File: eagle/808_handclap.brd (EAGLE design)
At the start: 100 x 80 mm, 82 parts, among them IC1 LM339N, IC2 TL071P, IC3 TL071P, Q1 2N3906, Q2 2N3904, Q3 2N3906, Q4 2N3906, Q5 2N3904, Q6 2N3904, Q7 2N3904, U1 POWER, U22 BA6110SIL

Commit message: 88pct autorouted
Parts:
- R350, R356, R364, R367, R371: device TR808clone:0207/5V -> TR808clone:0207/7
- moved C138 5.24 mm to (26.7, 69.8), turned to 270 degrees
- moved C140 4.02 mm to (48.3, 17.8)
- moved R363 2.84 mm to (7.62, 53.3)
- moved C139 2.54 mm to (33.0, 67.3), turned to 270 degrees
- moved Q7 2.54 mm to (49.5, 25.4)
- moved C144 2.54 mm to (50.8, 12.7)
- moved R367 2.54 mm to (43.2, 17.8)
- moved R368 2.54 mm to (39.4, 22.9)
- moved R348 1.80 mm to (29.2, 69.8), turned to 270 degrees
- moved C143 1.80 mm to (31.8, 54.6)
- moved D71 1.80 mm to (58.4, 8.89)
- moved R373 1.80 mm to (30.5, 15.2)
- moved C142 1.80 mm to (68.6, 27.9), turned to 0 degrees
- moved TM3 1.27 mm to (19.1, 73.7), turned to 90 degrees
- moved R358 1.27 mm to (58.4, 25.4)
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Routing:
- net GND: track 391.3 -> 0.00 mm
- net +12V: track 315.0 -> 0.00 mm
- net -12V: track 262.2 -> 0.00 mm
- net N$92: track 211.9 -> 0.00 mm
- net N$75: track 52.3 -> 0.00 mm
- net N$78: track 39.0 -> 0.00 mm
- net N$42: track 33.5 -> 0.00 mm
- net N$68: track 29.5 -> 0.00 mm
- net N$73: track 29.2 -> 0.00 mm
- net N$72: track 28.1 -> 0.00 mm
- net N$49: track 27.4 -> 0.00 mm
- net N$74: track 25.4 -> 0.00 mm
- net N$40: track 24.3 -> 0.00 mm
- net N$10: track 20.9 -> 0.00 mm
- net N$97: track 19.8 -> 0.00 mm
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
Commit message: 88pct autorouted
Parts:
- R105: device TR808clone:0207/5V -> TR808clone:0207/2V
- R334: device TR808clone:0207/7 -> TR808clone:0309/10
- moved R357 20.9 mm to (86.4, 11.4), turned to 180 degrees
- moved R359 3.59 mm to (39.4, 8.89)
- moved C144 2.84 mm to (49.5, 10.2)
- moved Q1 1.80 mm to (45.7, 25.4)
- moved D68 1.27 mm to (41.9, 55.9)
- moved R346 1.27 mm to (34.3, 59.7)
- moved R367 1.27 mm to (43.2, 16.5)
- moved C136 1.27 mm to (44.5, 47.0)
- moved Q7 1.27 mm to (50.8, 25.4)
- turned Q4 to 90 degrees
- turned TM3 to 0 degrees

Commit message: manual mode
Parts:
- C142: device TR808clone:C025-025X050 -> TR808clone:C050-025X075
- D69, D70, D71: value 1N4148DO35-7 -> 1N4148DO35-10; device TR808clone:DO35-7 -> TR808clone:DO35-10
- R104, R200', R332, R348, R357, R366, R372, R378, R382: device TR808clone:0207/5V -> TR808clone:0207/7
- R352, R370: device TR808clone:0207/5V -> TR808clone:0309/10
- R356: device TR808clone:0207/7 -> TR808clone:0207/5V
- R359, R360, R373: device TR808clone:0309/10 -> TR808clone:0207/7
- R361, R369, R383: device TR808clone:0207/5V -> TR808clone:0207/2V
- R364: device TR808clone:0207/7 -> TR808clone:0309/10
- moved R357 27.4 mm to (59.7, 17.8), turned to 270 degrees
- moved R359 26.8 mm to (60.6, 25.3)
- moved R374 10.7 mm to (53.1, 32.6), turned to 270 degrees
- moved R373 4.49 mm to (31.1, 19.7), turned to 180 degrees
- moved R356 4.07 mm to (54.6, 14.6)
- moved R383 4.02 mm to (57.1, 35.6), turned to 90 degrees
- moved Q6 3.81 mm to (14.0, 61.0), turned to 180 degrees
- moved R358 3.59 mm to (61.0, 27.9)
- moved R363 3.59 mm to (10.2, 55.9)
- moved R368 3.59 mm to (41.9, 25.4)
- moved C141 2.84 mm to (86.4, 16.5), turned to 0 degrees
- moved R355 2.84 mm to (86.4, 21.6)
- moved WHITE_NORM 2.84 mm to (19.1, 38.1)
- moved R370 2.84 mm to (17.8, 61.0)
- moved C136 2.84 mm to (45.7, 49.5), turned to 90 degrees
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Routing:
- net GND: track 0.00 -> 537.8 mm, vias 0 -> 2
- net -12V: track 0.00 -> 224.4 mm
- net N$92: track 0.00 -> 215.8 mm
- net +12V: track 0.00 -> 140.6 mm
- net N$74: track 0.00 -> 60.3 mm
- net N$42: track 0.00 -> 51.2 mm
- net N$73: track 0.00 -> 40.2 mm
- net N$10: track 0.00 -> 38.5 mm
- net N$68: track 0.00 -> 29.1 mm
- net N$52: track 0.00 -> 26.4 mm
- net N$72: track 0.00 -> 25.6 mm
- net N$65: track 0.00 -> 25.3 mm
- net N$97: track 0.00 -> 21.2 mm
- net N$77: track 0.00 -> 18.6 mm
- net N$46: track 0.00 -> 18.1 mm
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
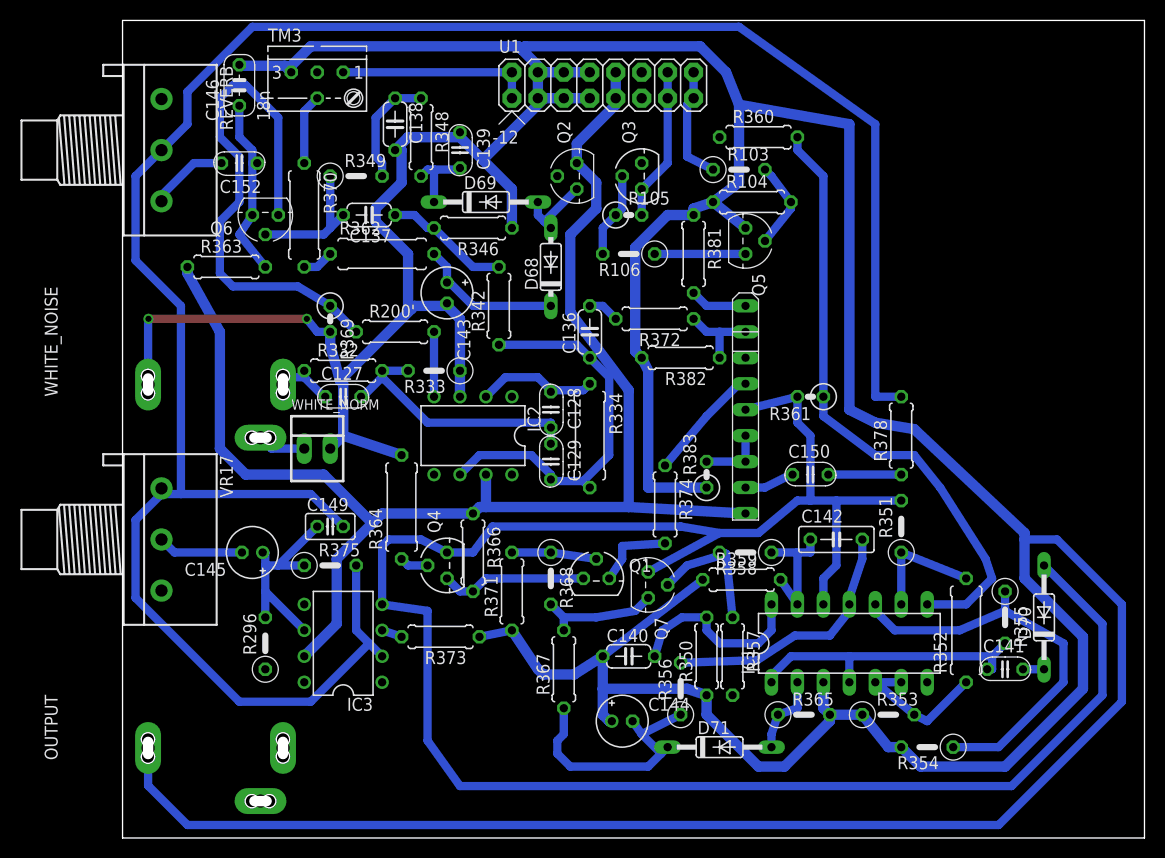
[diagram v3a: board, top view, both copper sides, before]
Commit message: more hand routes
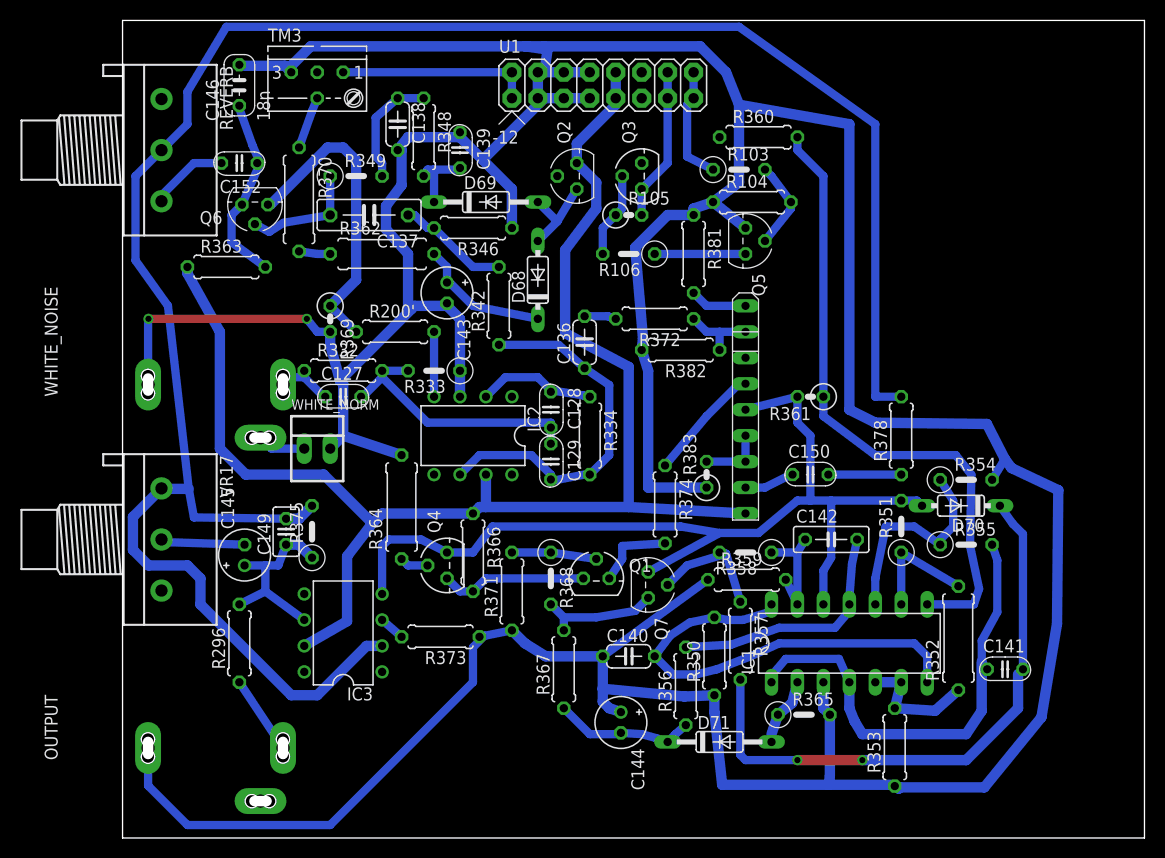
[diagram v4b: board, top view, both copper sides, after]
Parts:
- C137: device TR808clone:C050-024X044 -> TR808clone:C075-032X103
- D70: value 1N4148DO35-10 -> 1N4148DO35-7; device TR808clone:DO35-10 -> TR808clone:DO35-7
- R296, R353, R356: device TR808clone:0207/5V -> TR808clone:0207/7
- R334: device TR808clone:0309/10 -> TR808clone:0207/7
- moved R354 26.4 mm to (82.5, 35.1), turned to 0 degrees
- moved D70 13.6 mm to (82.0, 32.5), turned to 180 degrees
- moved R355 8.07 mm to (82.5, 28.7), turned to 0 degrees
- moved C149 4.35 mm to (16.0, 30.0), turned to 90 degrees
- moved R375 3.75 mm to (18.5, 30.0), turned to 90 degrees
- moved R353 3.24 mm to (75.6, 8.89), turned to 90 degrees
- moved R296 2.54 mm to (11.4, 19.1)
- moved D68 1.80 mm to (40.6, 54.6)
- moved R357 1.70 mm to (60.5, 19.3)
- moved R370 1.61 mm to (17.3, 62.5)
- moved Q6 1.44 mm to (13.0, 62.0)
- moved C136 1.14 mm to (45.2, 48.5)
- moved R352 1.08 mm to (81.8, 19.6)
- moved IC3 1.02 mm to (21.6, 20.1)
- moved C145 0.80 mm to (11.9, 27.7), turned to 90 degrees
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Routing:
- net -12V: track 224.4 -> 121.1 mm
- net GND: track 537.8 -> 468.1 mm
- net N$76: track 2.06 -> 57.7 mm, vias 0 -> 2
- net N$77: track 18.6 -> 44.6 mm
- net N$42: track 51.2 -> 30.3 mm
- net N$73: track 40.2 -> 20.9 mm
- net N$68: track 29.1 -> 46.5 mm
- net N$92: track 215.8 -> 203.8 mm
- net N$65: track 25.3 -> 13.8 mm
- net N$1: track 0.00 -> 7.72 mm
- net N$97: track 21.2 -> 18.6 mm
- net N$74: track 60.3 -> 62.5 mm
- net N$64: track 14.3 -> 12.2 mm
- net N$40: track 13.5 -> 11.7 mm
- net N$49: track 6.88 -> 5.14 mm
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
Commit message: routed
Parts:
- C127: device TR808clone:C035-025X75 -> TR808clone:C075-032X103
- C145: device TR808clone:E2-5 -> TR808clone:E3,5-8
- C149: device TR808clone:C025-025X050 -> TR808clone:C050-024X044
- R103, R368: device TR808clone:0207/5V -> TR808clone:0207/7
- R105: device TR808clone:0207/2V -> TR808clone:0207/5V
- R369: device TR808clone:0207/2V -> TR808clone:0207/7
- R381, R382: device TR808clone:0207/7 -> TR808clone:0207/5V
- moved R360 5.00 mm to (57.7, 66.5)
- moved R369 3.66 mm to (18.3, 53.8), turned to 180 degrees
- moved Q2 3.30 mm to (41.1, 64.8), turned to 0 degrees
- moved R349 3.10 mm to (20.3, 66.5), turned to 90 degrees
- moved R103 3.07 mm to (59.1, 62.6)
- moved Q5 2.75 mm to (59.4, 56.1)
- moved R378 2.54 mm to (73.7, 39.4)
- moved R334 2.17 mm to (43.7, 38.6)
- moved R106 2.09 mm to (50.0, 55.1)
- moved R375 2.05 mm to (20.6, 29.7)
- moved R104 2.05 mm to (61.3, 60.2)
- moved R363 1.83 mm to (11.7, 54.9), turned to 90 degrees
- moved R381 1.78 mm to (55.9, 55.4)
- moved C149 1.48 mm to (17.3, 29.2)
- moved R368 1.48 mm to (41.1, 24.1)
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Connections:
- net N$52: now also C127.2; no longer C127.P$2
- net WN: now also C127.1; no longer C127.P$1
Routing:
- net N$48: track 5.87 -> 100.6 mm, vias 0 -> 2
- net -12V: track 121.1 -> 189.9 mm, vias 0 -> 2
- net N$43: track 0.00 -> 14.0 mm
- net GND: track 468.1 -> 461.9 mm, vias 2 -> 4
- net N$42: track 30.3 -> 24.2 mm
- net N$46: track 18.9 -> 14.1 mm
- net TRIG: track 15.0 -> 18.9 mm
- net CP: track 11.4 -> 14.6 mm
- net N$78: track 11.8 -> 8.98 mm
- net N$44: track 9.09 -> 6.47 mm
- net N$62: track 7.14 -> 4.60 mm
- net N$52: track 26.4 -> 24.0 mm
- net N$60: track 11.4 -> 13.8 mm
- net N$37: track 8.41 -> 10.6 mm
- net N$3: track 8.89 -> 6.86 mm
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
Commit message: tweaks
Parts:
- R383: device TR808clone:0207/2V -> TR808clone:0207/7
- moved R383 6.14 mm to (56.4, 41.9), turned to 270 degrees
- moved R382 1.80 mm to (52.6, 48.3)
- moved R372 1.63 mm to (50.8, 51.1)
- moved R374 1.27 mm to (51.8, 32.9)
- moved R103 1.02 mm to (60.1, 62.6)
- moved R366 0.92 mm to (35.1, 28.4)
- moved Q1 0.80 mm to (46.1, 25.7)
- moved R334 0.51 mm to (43.7, 39.1)
- moved R359 0.51 mm to (61.6, 25.3)
- moved C128 0.25 mm to (41.1, 41.1)
- moved R369 0.25 mm to (18.5, 53.8)
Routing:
- net GND: track 461.9 -> 450.3 mm
- net N$60: track 13.8 -> 15.0 mm
- net N$67: track 14.3 -> 13.2 mm
- net N$61: track 6.36 -> 7.29 mm
- net N$56: track 7.92 -> 8.84 mm
- net CP: track 14.6 -> 13.7 mm
- net N$55: track 2.82 -> 2.05 mm
- net N$68: track 45.4 -> 44.6 mm
- net N$48: track 100.6 -> 99.9 mm
- net N$4: track 9.13 -> 8.51 mm
- net N$54: track 11.5 -> 10.9 mm
- net N$69: track 6.25 -> 5.72 mm
- net +12V: track 140.1 -> 139.6 mm
